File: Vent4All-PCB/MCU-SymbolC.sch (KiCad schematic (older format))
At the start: 1 part, among them U1 NUCLEO-F429ZI

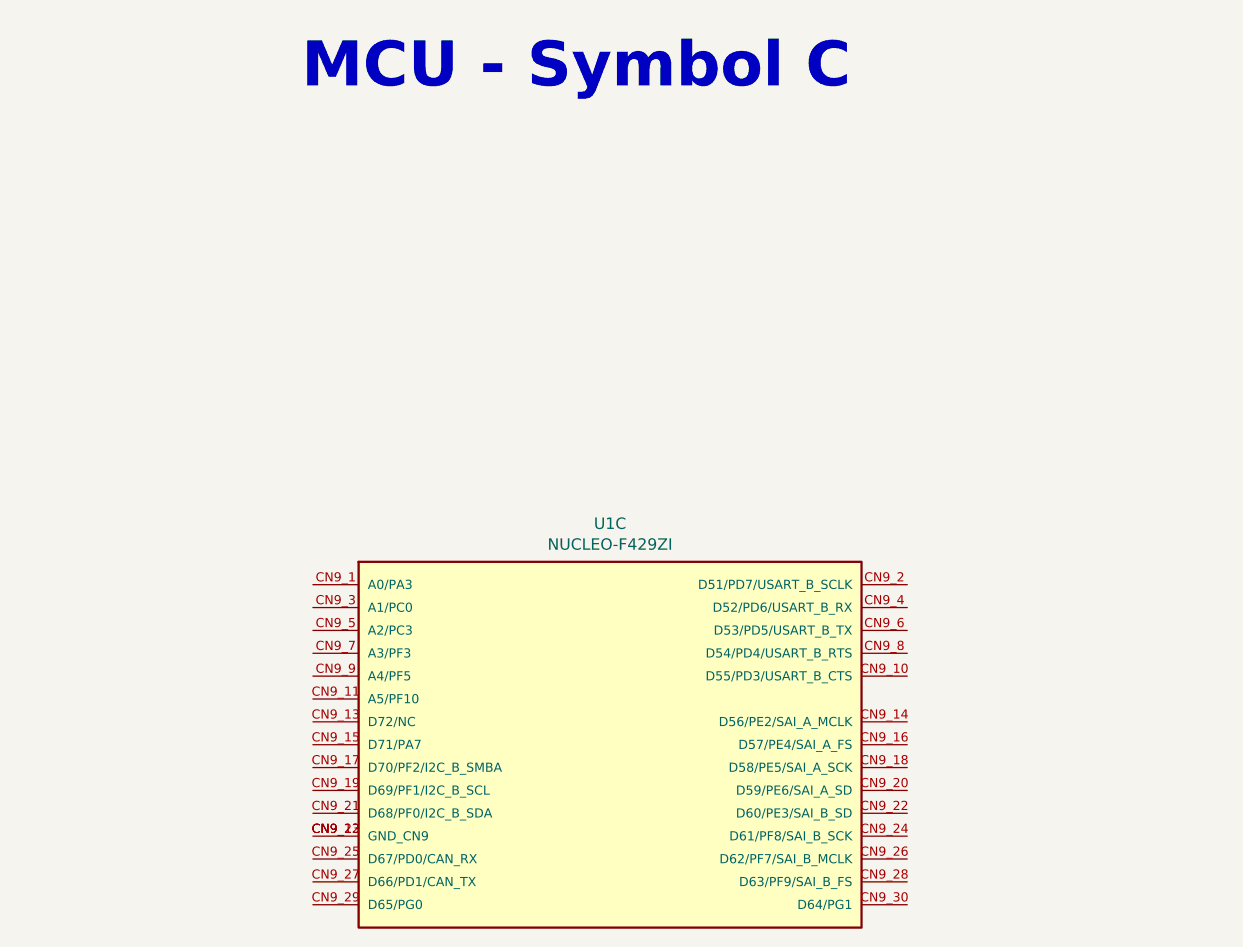
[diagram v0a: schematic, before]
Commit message: Added global labels for reserved communication lines (SPI, I2C, UARTs).
Added hierarchical sheet for external connection interfaces (e.g. to RPi).
Changed symbol libraries table to use ${KIPRJMOD} instead of absolute paths.
When I imported the schematic, KiCAD made a rescue library and changed the line endings of all the .sch files.
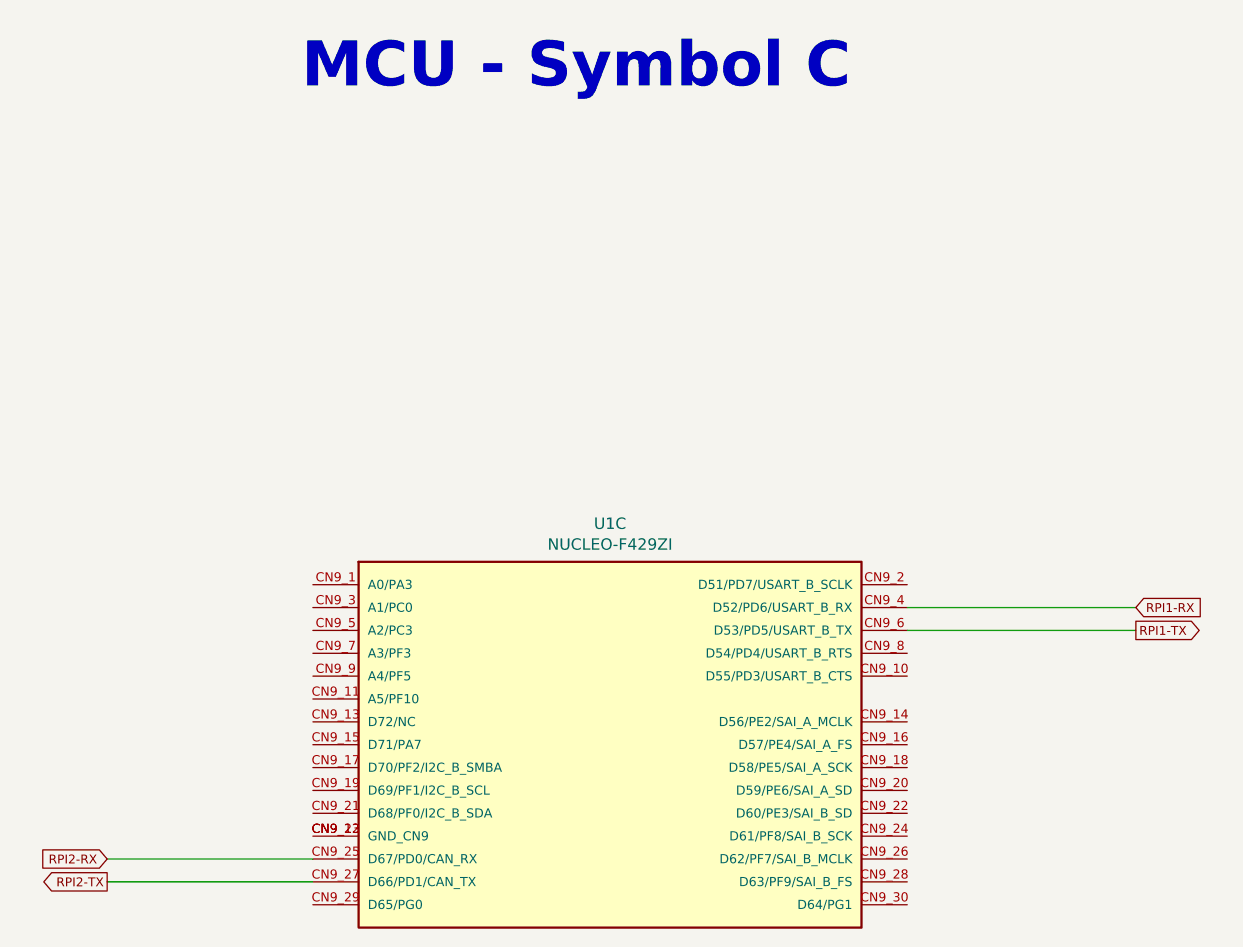
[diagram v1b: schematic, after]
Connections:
- net RPI2-RX: now reaches U1.CN9_25 (D67/PD0/CAN_RX)
- net RPI2-TX: now reaches U1.CN9_27 (D66/PD1/CAN_TX)
- net RPI1-RX: now reaches U1.CN9_4 (D52/PD6/USART_B_RX)
- net RPI1-TX: now reaches U1.CN9_6 (D53/PD5/USART_B_TX)
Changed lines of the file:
@@
 Text Notes 4350 1100 0    197  ~ 39
 MCU - Symbol C
+Text GLabel 3500 4450 0    39   Input ~ 0
+RPI2-RX
+Text GLabel 3500 4550 0    39   Output ~ 0
+RPI2-TX
+Wire Wire Line
+	3500 4450 4400 4450
+Wire Wire Line
+	3500 4550 4400 4550
+Text GLabel 8000 3350 2    39   Input ~ 0
+RPI1-RX
+Text GLabel 8000 3450 2    39   Output ~ 0
+RPI1-TX
+Wire Wire Line
+	8000 3450 7000 3450
+Wire Wire Line
+	7000 3350 8000 3350
 $EndSCHEMATC
